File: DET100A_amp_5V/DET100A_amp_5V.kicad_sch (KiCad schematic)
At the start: 14 parts, among them J1 5227677-1, J2 Screw_Terminal_01x03, J3 5227677-1, U1 OPA656NB/250

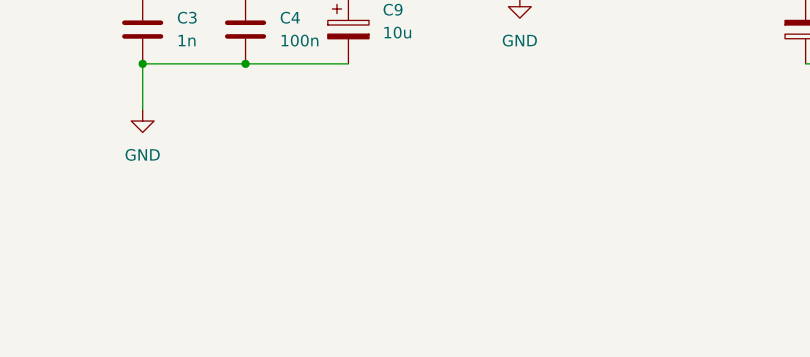
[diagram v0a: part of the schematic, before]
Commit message: feat(PCB): add TPs for the 5V version
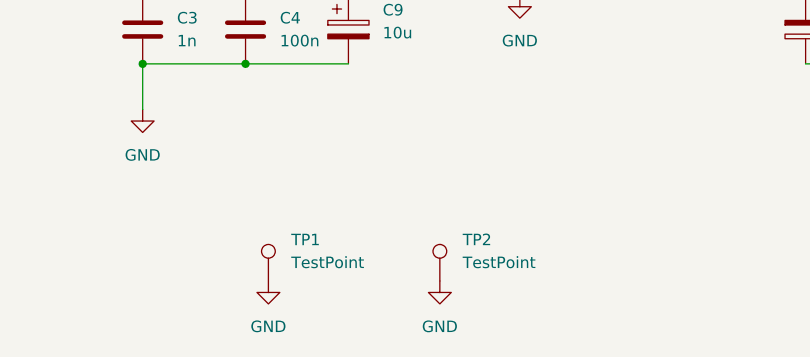
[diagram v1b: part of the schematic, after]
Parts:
- added TP1, TP2: TestPoint, Charlie:TestPoint_THTPad_D2.0mm_Drill1.0mm, symbol Connector:TestPoint
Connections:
- net GND: now also TP1.1, TP2.1
